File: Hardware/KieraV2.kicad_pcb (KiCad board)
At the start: 2 copper layers, 121.7 x 50.3 mm, 85 parts, among them J1 Conn_01x04_Male, J2 Conn_01x05_Male, SW1 SW_Rotary2x4, SW2 SW_Rotary2x4, SW3 SW_Push, SW4 SW_Push, SW5 SW_Push, SW6 SW_Push, SW7 SW_MEC_5G, U1 STM32L4P5RET6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

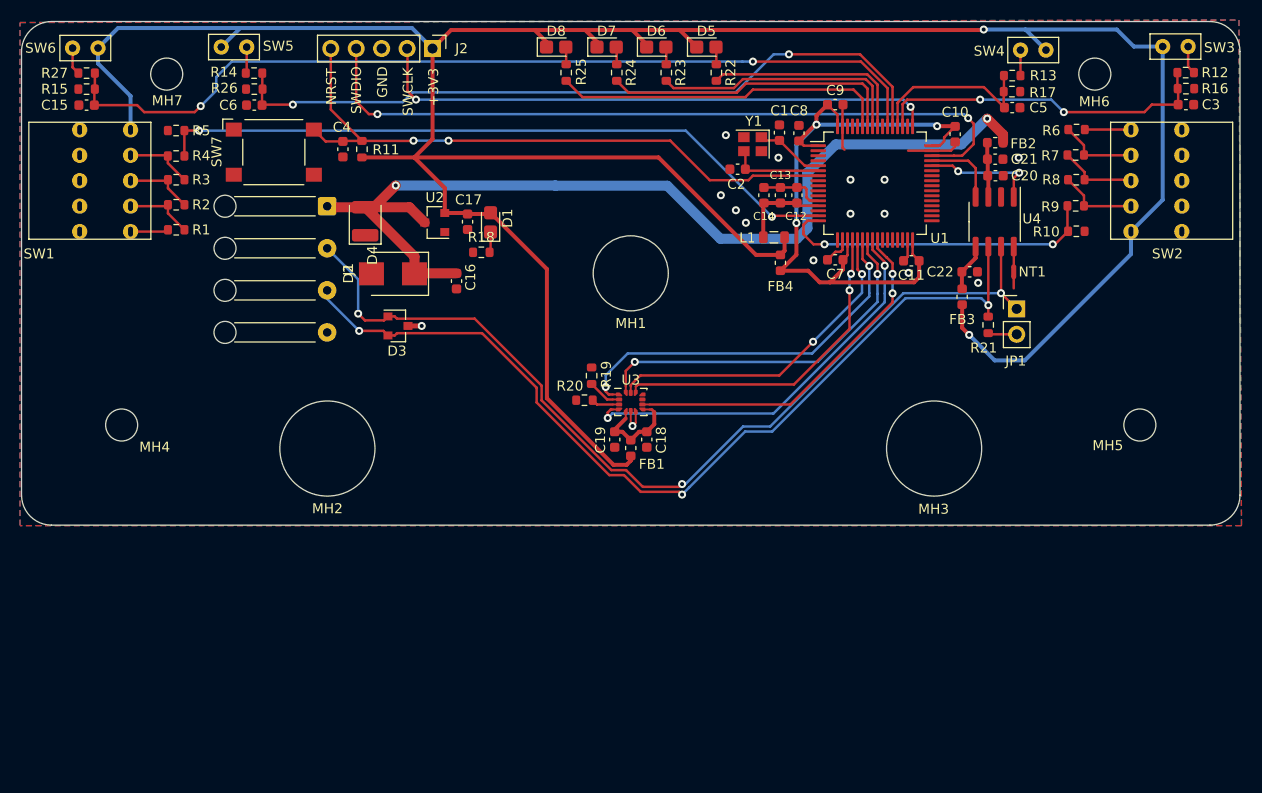
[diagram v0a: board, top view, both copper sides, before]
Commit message: added logos
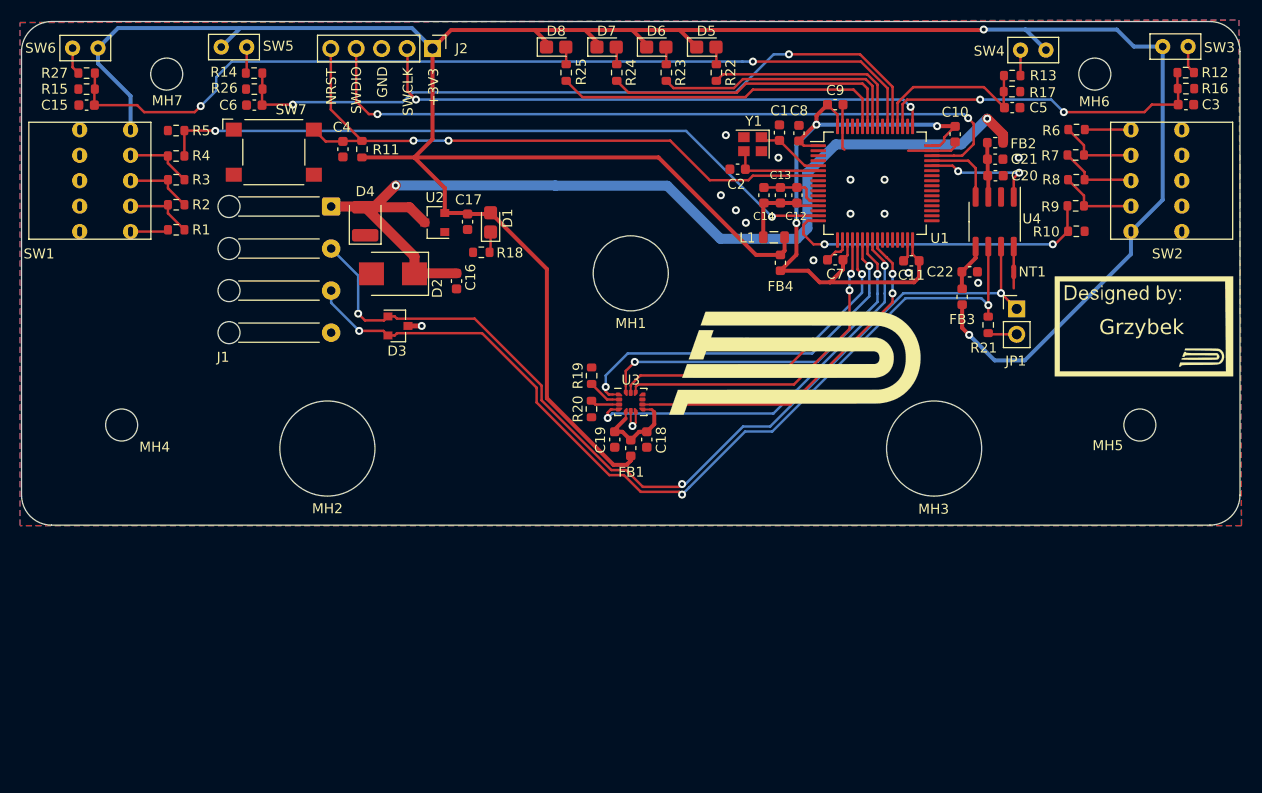
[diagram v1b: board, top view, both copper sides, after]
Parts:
- added G***: LOGO, Logos:PUTM_LOGO_30mm, F.Cu at (174.1, 112.2)
- added G***: LOGO, Logos:myLogo, F.Cu at (209.5, 108.8)
- moved R20 1.12 mm to (154.5, 117.1), turned to 90 degrees
- moved J1 0.40 mm to (128.5, 96.9)
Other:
- board text added: "Grzybek"

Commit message: rtr
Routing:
- net /CAN+: track 96.2 -> 95.3 mm
- net /CAN-: track 91.3 -> 90.4 mm
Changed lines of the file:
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@@
     (thickness 1.6)
     (drawings 36)
-    (tracks 549)
+    (tracks 541)
     (zones 0)
     (modules 87)
@@
   (segment (start 164.271447 124.953553) (end 163.575 125.65) (width 0.25) (layer B.Cu) (net 88))
   (segment (start 169.874999 119.350001) (end 164.271447 124.953553) (width 0.25) (layer B.Cu) (net 88))
-  (segment (start 159.446446 125.375) (end 163.3 125.375) (width 0.25) (layer F.Cu) (net 88))
-  (segment (start 156.305431 123.705001) (end 157.776447 123.705001) (width 0.25) (layer F.Cu) (net 88))
-  (segment (start 149.050001 116.449571) (end 156.305431 123.705001) (width 0.25) (layer F.Cu) (net 88))
-  (segment (start 149.050001 114.978555) (end 149.050001 116.449571) (width 0.25) (layer F.Cu) (net 88))
-  (segment (start 163.3 125.375) (end 163.575 125.65) (width 0.25) (layer F.Cu) (net 88))
-  (segment (start 157.776447 123.705001) (end 159.446446 125.375) (width 0.25) (layer F.Cu) (net 88))
-  (segment (start 134.875001 109.755) (end 135.1 109.530001) (width 0.25) (layer F.Cu) (net 88))
-  (segment (start 134.2 109.755) (end 134.875001 109.755) (width 0.25) (layer F.Cu) (net 88))
-  (segment (start 143.601447 109.530001) (end 149.050001 114.978555) (width 0.25) (layer F.Cu) (net 88))
-  (segment (start 135.1 109.530001) (end 143.601447 109.530001) (width 0.25) (layer F.Cu) (net 88))
   (segment (start 128.525 106.5) (end 131.325 109.3) (width 0.25) (layer B.Cu) (net 88))
   (segment (start 128.525 105.275) (end 128.525 106.5) (width 0.25) (layer B.Cu) (net 88))
+  (segment (start 135.124999 109.530001) (end 139.593591 109.530001) (width 0.25) (layer F.Cu) (net 88))
+  (segment (start 134.2 109.755) (end 134.9 109.755) (width 0.25) (layer F.Cu) (net 88))
+  (segment (start 139.593591 109.530001) (end 155.713589 125.65) (width 0.25) (layer F.Cu) (net 88))
+  (segment (start 155.713589 125.65) (end 163.009315 125.65) (width 0.25) (layer F.Cu) (net 88))
+  (segment (start 134.9 109.755) (end 135.124999 109.530001) (width 0.25) (layer F.Cu) (net 88))
+  (segment (start 163.009315 125.65) (end 163.575 125.65) (width 0.25) (layer F.Cu) (net 88))
   (segment (start 195.435 100.875) (end 195.435 101.785) (width 0.25) (layer F.Cu) (net 89))
   (segment (start 195.435 105.535) (end 195.435 105.535) (width 0.25) (layer F.Cu) (net 89))
@@
   (segment (start 185.688002 105.535) (end 172.372992 118.85001) (width 0.25) (layer B.Cu) (net 89))
   (segment (start 195.435 105.535) (end 185.688002 105.535) (width 0.25) (layer B.Cu) (net 89))
-  (segment (start 134.2 107.855) (end 134.875001 107.855) (width 0.25) (layer F.Cu) (net 89))
-  (segment (start 163.3 124.875) (end 163.575 124.6) (width 0.25) (layer F.Cu) (net 89))
-  (segment (start 134.875001 107.855) (end 135.1 108.079999) (width 0.25) (layer F.Cu) (net 89))
-  (segment (start 149.54999 114.771436) (end 149.549991 116.242467) (width 0.25) (layer F.Cu) (net 89))
-  (segment (start 149.549991 116.242467) (end 156.512534 123.20501) (width 0.25) (layer F.Cu) (net 89))
-  (segment (start 156.512534 123.20501) (end 157.983564 123.20501) (width 0.25) (layer F.Cu) (net 89))
-  (segment (start 157.983564 123.20501) (end 159.653554 124.875) (width 0.25) (layer F.Cu) (net 89))
-  (segment (start 159.653554 124.875) (end 163.3 124.875) (width 0.25) (layer F.Cu) (net 89))
-  (segment (start 142.858553 108.079999) (end 149.54999 114.771436) (width 0.25) (layer F.Cu) (net 89))
-  (segment (start 135.1 108.079999) (end 142.858553 108.079999) (width 0.25) (layer F.Cu) (net 89))
   (segment (start 131.225 103.775) (end 131.225 104.375) (width 0.25) (layer B.Cu) (net 89))
   (segment (start 128.525 101.075) (end 131.225 103.775) (width 0.25) (layer B.Cu) (net 89))
   (segment (start 131.225 104.375) (end 131.225 107.575) (width 0.25) (layer B.Cu) (net 89))
   (segment (start 131.225 104.15) (end 131.225 104.375) (width 0.25) (layer B.Cu) (net 89))
+  (segment (start 155.575 124.875) (end 163.3 124.875) (width 0.25) (layer F.Cu) (net 89))
+  (segment (start 138.779999 108.079999) (end 155.575 124.875) (width 0.25) (layer F.Cu) (net 89))
+  (segment (start 135.1 108.079999) (end 138.779999 108.079999) (width 0.25) (layer F.Cu) (net 89))
+  (segment (start 134.875001 107.855) (end 135.1 108.079999) (width 0.25) (layer F.Cu) (net 89))
+  (segment (start 134.2 107.855) (end 134.875001 107.855) (width 0.25) (layer F.Cu) (net 89))
+  (segment (start 163.3 124.875) (end 163.575 124.6) (width 0.25) (layer F.Cu) (net 89))
   (segment (start 104.925 83.55) (end 104.925 85.15) (width 0.25) (layer F.Cu) (net 90))
   (segment (start 104.875 85.2) (end 104.925 85.15) (width 0.25) (layer F.Cu) (net 90))

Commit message: pcb changed
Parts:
- removed MH6: MountingHole_3.2mm_M3, MountingHole:MountingHole_3.2mm_M3
- added MHe: MountingHole_3.2mm_M3, MountingHole:MountingHole_3.2mm_M3, F.Cu at (188.4, 96.0)
- moved MH1 38.5 mm to (158.0, 142.1)
- moved SW7 34.8 mm to (142.0, 120.5), turned to 270 degrees
- moved R21 34.0 mm to (174.7, 136.6)
- moved JP1 33.7 mm to (177.9, 134.8)
- moved C16 33.1 mm to (143.4, 137.3)
- moved D2 33.1 mm to (137.0, 136.6)
- moved D3 33.1 mm to (137.5, 141.8)
- moved D4 33.1 mm to (134.2, 131.3)
- moved J1 33.1 mm to (130.8, 129.8)
- moved C20 33.0 mm to (174.9, 120.1)
- moved C21 33.0 mm to (174.8, 118.5)
- moved FB2 33.0 mm to (174.8, 116.8)
- moved FB3 33.0 mm to (171.6, 132.2)
- moved U4 33.0 mm to (174.8, 124.7)
- moved C22 33.0 mm to (172.3, 129.7)
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- renumbered MH2 to MHe
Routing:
- net +3V3: track 284.5 -> 177.4 mm, vias 2 -> 1
- net /NRST: track 63.2 -> 29.5 mm, vias 2 -> 0
- net /SW4: track 17.8 -> 51.3 mm, vias 0 -> 2
- net +5V: track 99.4 -> 67.6 mm
- net /SWDIO: track 74.6 -> 46.9 mm
- net /SW3: track 34.0 -> 61.2 mm
- net /ControlLED4: track 33.7 -> 9.74 mm
- net /SW1: track 69.5 -> 46.4 mm
- net /CAN-: track 90.4 -> 68.0 mm, vias 3 -> 2
- net /CAN+: track 95.3 -> 73.0 mm
- net /ControlLED3: track 29.9 -> 8.10 mm
- net /IMU_INT1: track 41.0 -> 19.3 mm
- net /IMU_SPI1_CS: track 33.4 -> 11.8 mm
- net /SWCLK: track 57.2 -> 35.7 mm
- net /IMU_SPI1_MISO: track 38.6 -> 17.3 mm, vias 2 -> 4
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- removed copper zone on B.Cu, net GND
- removed copper zone on F.Cu, net GND
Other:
- board size 121.7 x 50.3 mm -> 111 x 63.2 mm

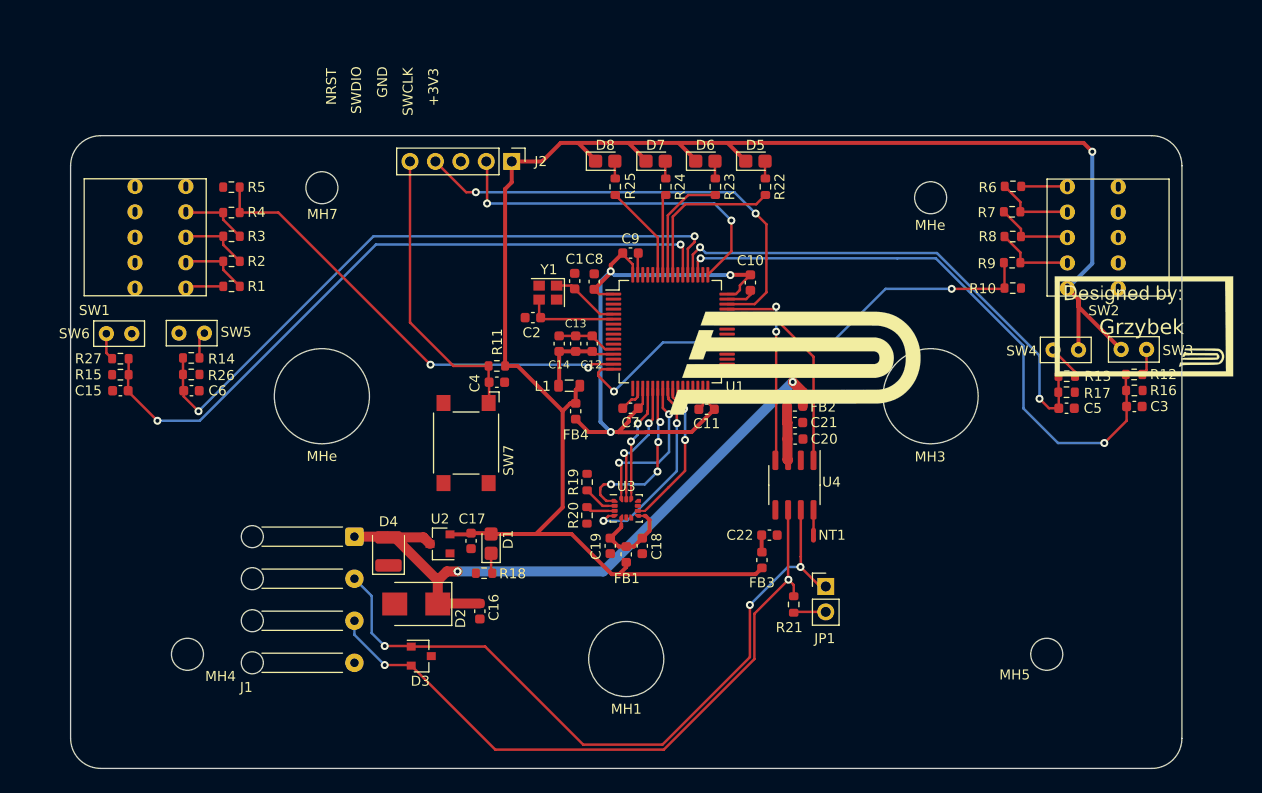
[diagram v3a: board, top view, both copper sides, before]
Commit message: added logos
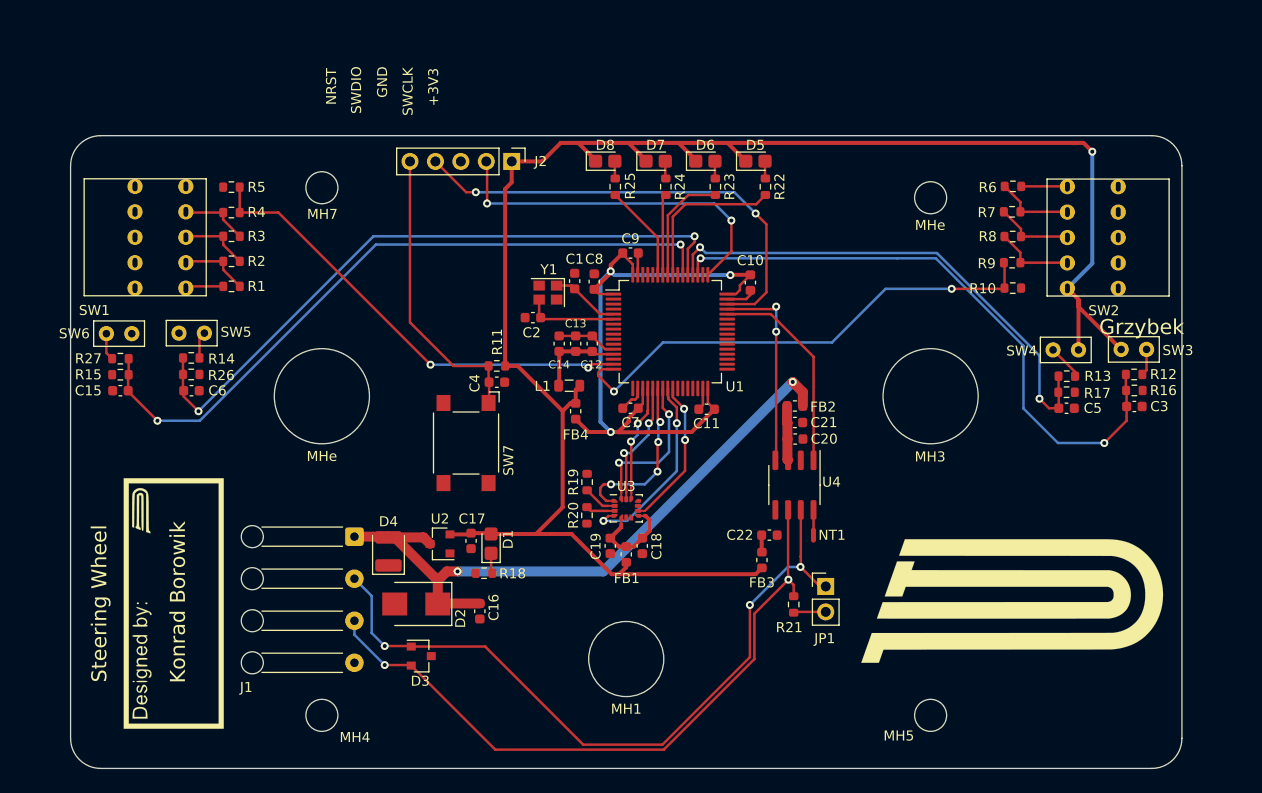
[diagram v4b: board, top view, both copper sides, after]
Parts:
- removed the G*** at (174.1, 112.2)
- removed the G*** at (209.5, 108.8)
- added G***: LOGO, Logos:SignatureBox25mm, F.Cu at (112.8, 136.6)
- added G***: LOGO, Logos:PUTM_LOGO_35mm, F.Cu at (195.6, 135.9)
- moved MH4 14.7 mm to (127.6, 147.7)
- moved MH5 13.1 mm to (188.4, 147.7)
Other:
- board text added: "Konrad Borowik"
- board text added: "Steering Wheel"

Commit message: new changes
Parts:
- moved R14 2.38 mm to (113.0, 113.8)
- moved C6 2.38 mm to (113.0, 117.1)
- moved R26 2.38 mm to (113.0, 115.5)
- moved SW5 1.99 mm to (113.7, 111.3)
- moved C15 1.75 mm to (107.6, 117.0)
- moved R15 1.75 mm to (107.6, 113.8)
- moved R27 1.75 mm to (107.6, 115.4)
- moved SW6 1.75 mm to (107.4, 111.3)
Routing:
- net +3V3: track 177.4 -> 234.7 mm
- net /SW5: track 66.9 -> 69.2 mm
- net /SW6: track 70.1 -> 71.0 mm
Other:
- board text removed: "Grzybek"

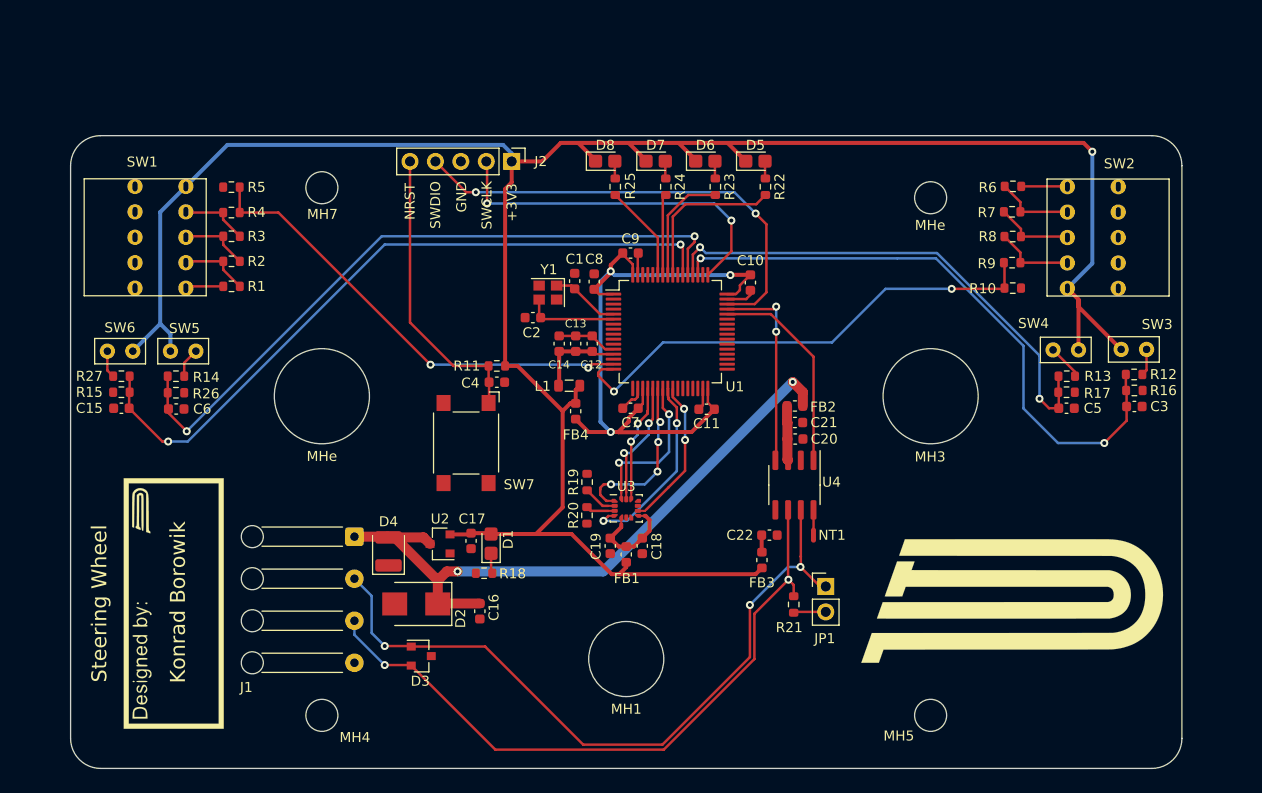
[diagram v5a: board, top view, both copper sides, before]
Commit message: added gnd layers
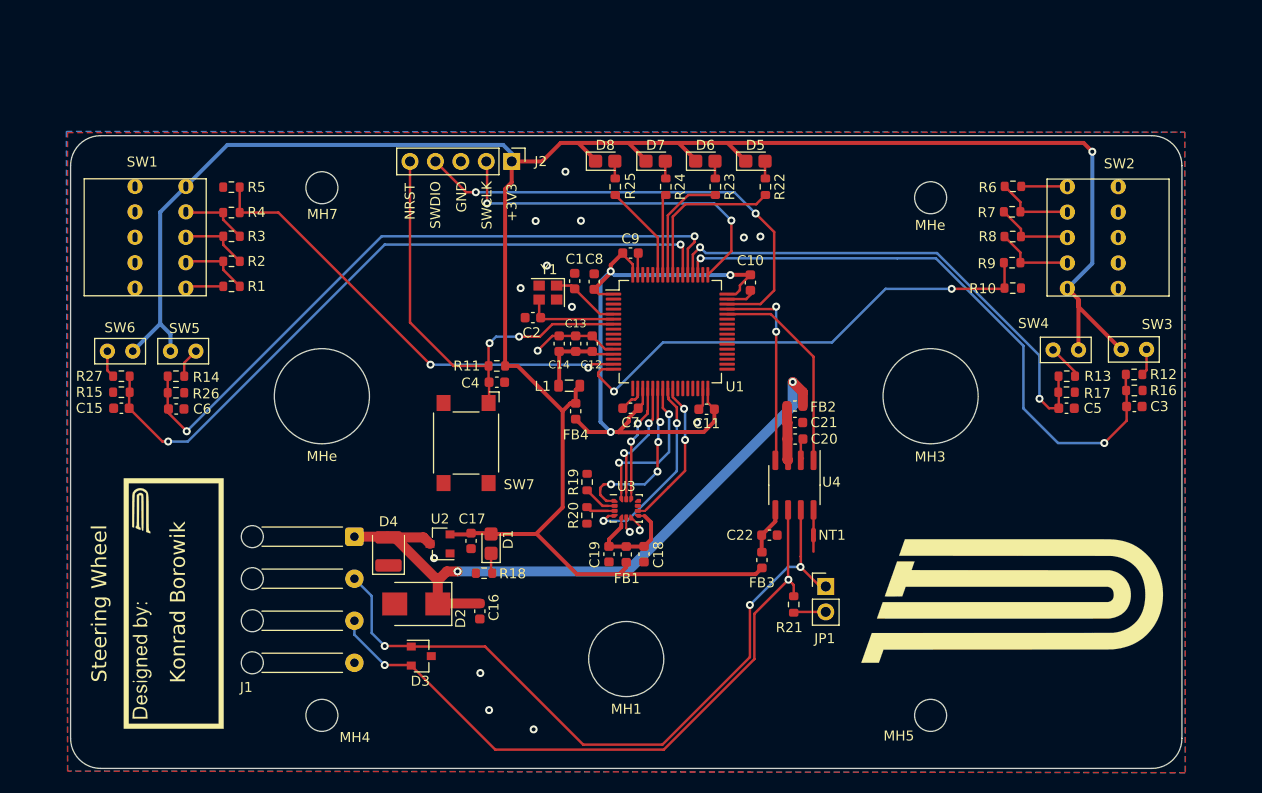
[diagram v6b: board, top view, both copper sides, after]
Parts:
- moved C18 0.84 mm to (159.8, 131.6)
- moved C19 0.83 mm to (156.3, 131.6)
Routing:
- net /NRST: track 29.5 -> 44.9 mm, vias 0 -> 2
- net GND: track 16.2 -> 25.8 mm, vias 0 -> 16
- net /CAN/+3V3_VIO: track 1.71 -> 4.80 mm
- net +5V: track 67.6 -> 69.0 mm
- net /IMU/+3.3V_IMU: track 9.87 -> 11.2 mm
- net /SWDIO: track 46.9 -> 47.8 mm
- net /+3V3_uC: track 67.0 -> 67.7 mm
- added copper zone on B.Cu, net GND
- added copper zone on F.Cu, net GND

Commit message: wip
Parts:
- U3: footprint Package_LGA:LGA-14_3x2.5mm_P0.5mm_LayoutBorder3x4y -> PUTM_Kicad_FOOTPRINTS:LGA-14_3x2.5mm_P0.5mm_LayoutBorder3x4y
